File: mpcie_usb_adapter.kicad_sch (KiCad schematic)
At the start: 14 parts, among them J1 USB4105-GF-A, J2 SMA-J-P-H-ST-EM1, J3 SMA-J-P-H-ST-EM1, J4 Conn_Coaxial_Small, J5 Conn_Coaxial_Small, U1 LD1117S33TR, U2 AS-RTK2B-MPCIE-L1L2-F9P-01

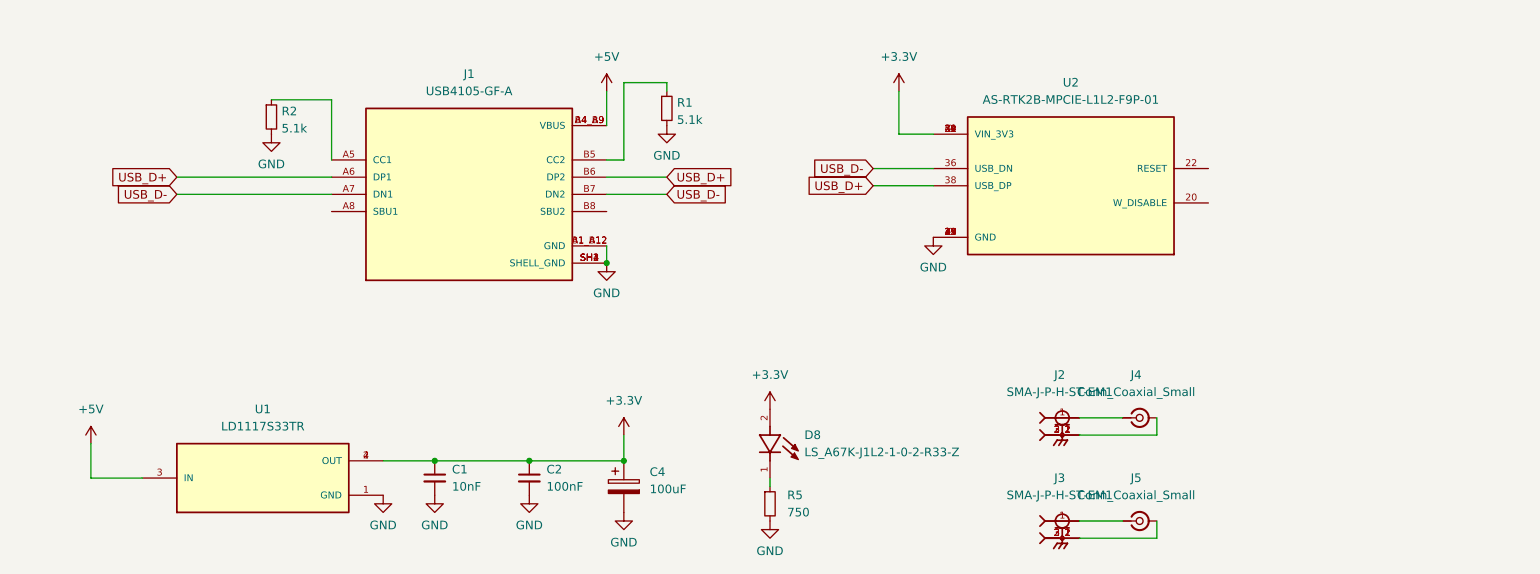
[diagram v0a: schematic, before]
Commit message: added ESD protection diodes and capacitors
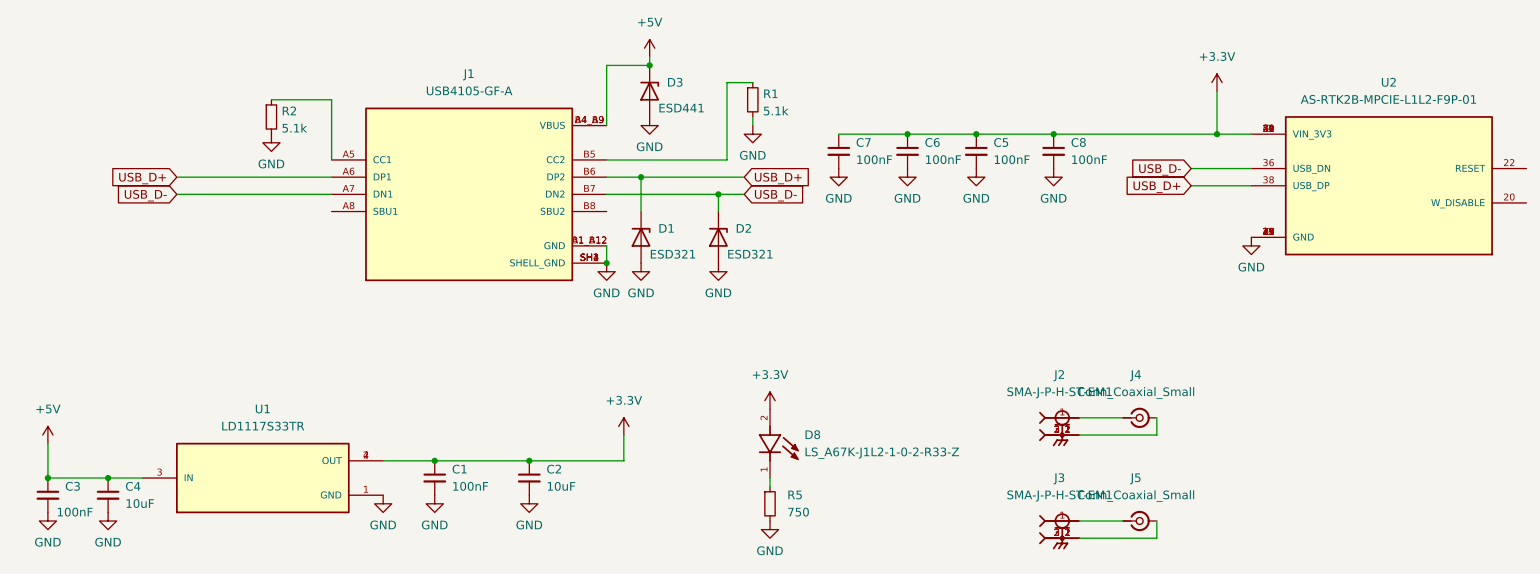
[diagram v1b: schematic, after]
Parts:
- removed C4: 100uF, Capacitor_SMD:CP_Elec_6.3x5.4, symbol Device:C_Polarized
- added C3, C5, C6, C7, C8: 100nF, Capacitor_SMD:C_0805_2012Metric, symbol Device:C_Small
- added C4: 10uF, Capacitor_SMD:C_0805_2012Metric, symbol Device:C_Small
- added D1, D2: ESD321, Diode_SMD:D_SOD-523, symbol Diode:ESD5Zxx
- added D3: ESD441, Diode_SMD:D_SOD-523, symbol Diode:ESD5Zxx
- C1: value 10nF -> 100nF
- C2: value 100nF -> 10uF
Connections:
- net +3.3V: now also C5.1, C6.1, C7.1, C8.1
- net +5V: now also C3.1, C4.1, D3.1 (K)
- net GND: now also C3.2, C4.2, C5.2, C6.2, C7.2, C8.2, D1.2 (A), D2.2 (A), D3.2 (A)
- net USB_D+: now also D1.1 (K)
- net USB_D-: now also D2.1 (K)
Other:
- moved on the sheet: R1, U2

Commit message: reworked pcb
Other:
- moved on the sheet: C3, C4, D1, D2, D3, J1, R1, R2
